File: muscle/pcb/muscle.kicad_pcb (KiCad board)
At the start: 4 copper layers, 135 x 50 mm, 176 parts, among them J1 B4B-XH-2(LF)(SN), J10 USB4115-03-C, J2 WAFER-SH1.0-3PWB, J4 WAFER-SH1.0-3PWB, J5 B4B-XH-2(LF)(SN), J8 B2B-XH-A(LF)(SN), J9 USB4115-03-C, Q1 AO3401A, Q10 BSS138W, Q2 AONR21321, Q3 WSD6070DN56, Q4 WSD6070DN56, Q5 BSS138W, Q6 WSD6070DN56, Q7 AONR21321, Q8 WSD6070DN56, Q9 AGM18N10AP, SW1 TS3425BA, SW2 TS3425BA, U1 TMC2209-LA, U11 TPS563300, U13 TLV75733PDBV, U14 DRV8701P, U2 TMC2209-LA, U3 RP2350A, U4 CYPD3177-24LQ, U5 LM5156, U6 W25Q128JVSS, U7 LM393BIDSGR, U8 TUSB320, U9 TPS2041BDBV, Y1 ABM8-272-T3

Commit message: muscle: switch to side buttons for RESET and BOOT
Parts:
- SW1, SW2: value TS3425BA -> TS24CA; footprint Button_Switch_SMD:SW_Push_1P1T_NO_Vertical_Wuerth_434133025816 -> Button_Switch_SMD:Panasonic_EVQPUL_EVQPUC
- moved J2 17.6 mm to (194.7, 95.6)
- moved R7 12.6 mm to (188.4, 116.0)
- moved R19 11.8 mm to (192.5, 109.2), turned to -90 degrees
- moved SW1 10.2 mm to (195.5, 113.5), turned to -90 degrees
- moved R13 9.97 mm to (187.2, 116.0)
- moved SW2 9.29 mm to (195.5, 105.5)
- moved R18 5.20 mm to (182.3, 94.6), turned to 180 degrees
- moved J4 1.85 mm to (194.7, 88.0)
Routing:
- net /QSPI_SS: track 44.9 -> 19.5 mm, vias 2 -> 0
- net /DBG_TX: track 8.14 -> 22.8 mm
- net /RESET: track 36.2 -> 46.8 mm, vias 2 -> 4
- net /~{USB_BOOT}: track 5.59 -> 15.0 mm, vias 0 -> 2
- net /DBG_RX: track 12.9 -> 18.4 mm
- net GND: track 159.2 -> 161.5 mm, vias 228 -> 227
- net /SWCLK: track 27.3 -> 28.1 mm
- net /SWD: track 28.3 -> 29.1 mm
- net /S_SENSE_COMP: track 9.68 -> 9.00 mm
- net Net-(U1-VREF): track 10.5 -> 9.90 mm

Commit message: muscle: use correct TUSB320LI model
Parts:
- U8: value TUSB320 -> TUSB320LI
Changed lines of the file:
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@@
 			)
 		)
-		(property "Value" "TUSB320"
+		(property "Value" "TUSB320LI"
 			(at 0.05 1.025 0)
 			(layer "F.Fab")
@@
 			)
 		)
-		(property "Datasheet" "http://www.ti.com/lit/ds/symlink/tusb320.pdf"
+		(property "Datasheet" "https://www.ti.com/lit/ds/symlink/tusb320li.pdf"
 			(at 0 0 0)
 			(layer "F.Fab")
@@
 			(hide yes)
 			(effects
+				(font
+					(size 1 1)
+					(thickness 0.15)
+				)
+			)
+		)
+		(property "LCSC" "C2836598"
+			(at 0 0 0)
+			(unlocked yes)
+			(layer "F.Fab")
+			(hide yes)
+			(effects

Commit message: muscle: USB protection
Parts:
- added U12: TPD2EUSB30A, Package_TO_SOT_SMD:Texas_DRT-3, F.Cu at (98.0, 100.2)
- moved R33 2.25 mm to (98.0, 97.3)
- moved D6 1.22 mm to (92.1, 97.3)
- moved C41 1.17 mm to (95.2, 94.3)
- moved U9 1.17 mm to (95.2, 97.0)
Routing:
- net /USB_D-: track 99.8 -> 107.1 mm
- net /USB_D+: track 103.2 -> 107.3 mm
- net GND: track 161.5 -> 164.4 mm, vias 227 -> 226
- net /USB_ROLE: track 104.3 -> 105.7 mm
- net /VBUS_DATA: track 25.6 -> 27.0 mm
- net +3V3: track 161.0 -> 159.7 mm
- net +5V: track 38.3 -> 39.5 mm
- net /~{DRV_EN}: track 130.4 -> 129.5 mm
- net /RESET: track 46.8 -> 46.0 mm
- net Net-(R19-Pad1): track 9.90 -> 9.32 mm

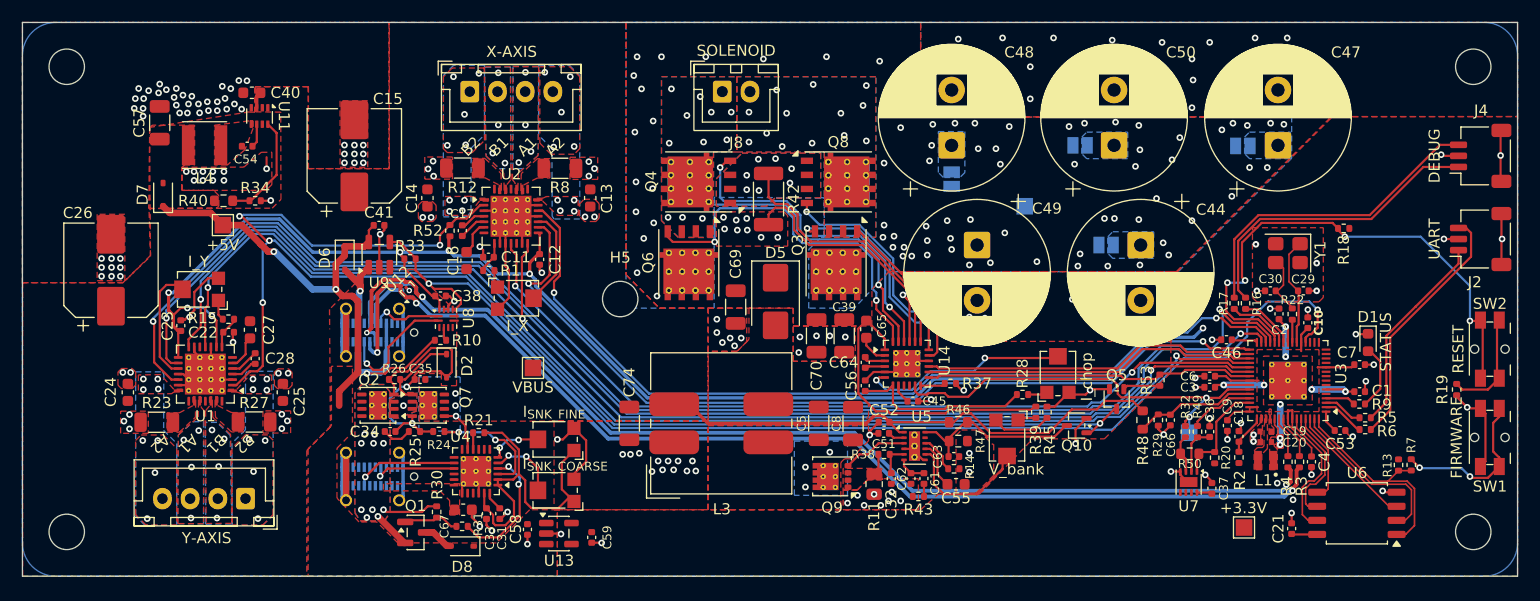
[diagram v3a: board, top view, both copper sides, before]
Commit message: muscle: replace USB PD power
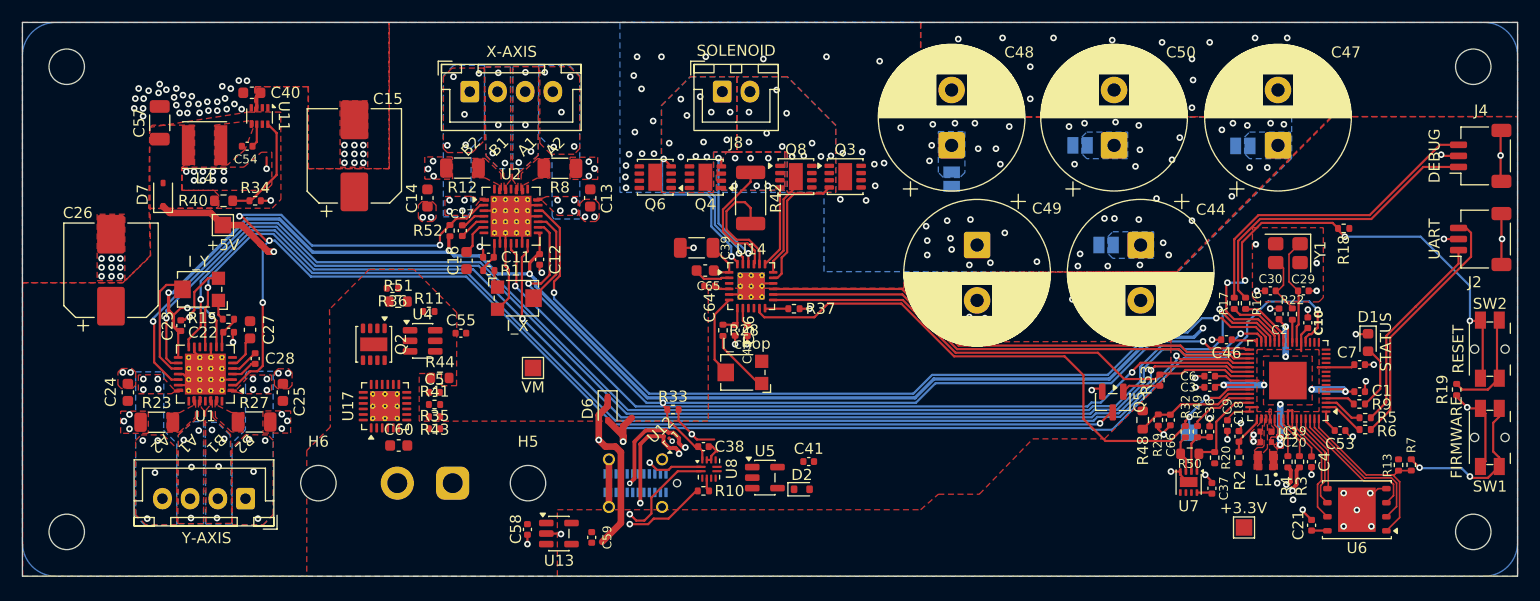
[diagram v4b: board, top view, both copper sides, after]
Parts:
- removed C31, C34, C35, C51, C52, C61: 1u, Capacitor_SMD:C_0402_1005Metric
- removed C32, C63: 100p, Capacitor_SMD:C_0402_1005Metric
- removed C33: 4.7u, Capacitor_SMD:C_0402_1005Metric
- removed C62: 22n, Capacitor_SMD:C_0402_1005Metric
- removed C67: 10u, Capacitor_SMD:C_0603_1608Metric
- removed C69, C70, C74: 10u, Capacitor_SMD:C_1206_3216Metric
- removed C8: 4.7u, Capacitor_SMD:C_1206_3216Metric
- removed D5: 100V,5A, Diode_SMD:D_SMB
- removed D8: ~, Diode_SMD:D_SOD-323
- removed J9: USB4115-03-C, Connector_USB:USB_C_Receptacle_GCT_USB4115-03-C
- removed L3: 33u,2.4A, Inductor_SMD:L_Bourns_SRF1260
- removed Q1: AO3401A, Package_TO_SOT_SMD:SOT-23
- removed Q10: BSS138W, Package_TO_SOT_SMD:SOT-323_SC-70
- removed Q7: AONR21321, Package_DFN_QFN:DFN-8-1EP_3x3mm_P0.65mm_EP1.6x2.56mm_ThermalVias
- removed Q9: AGM18N10AP, mainboard:VSON-8_3.3x3.3mm_P0.65mm_NexFET_Thermalvias
- removed R14: 51k, Resistor_SMD:R_0402_1005Metric
- removed R21, R26, R30: 50k, Resistor_SMD:R_0402_1005Metric
- removed R24, R31: 1k, Resistor_SMD:R_0402_1005Metric
- removed R25: 10k, Resistor_SMD:R_0402_1005Metric
- removed R38: 100, Resistor_SMD:R_0402_1005Metric
- removed R39: 200k, Resistor_SMD:R_0402_1005Metric
- removed R45: 5.1k, Resistor_SMD:R_0402_1005Metric
- removed R46: 68k, Resistor_SMD:R_0603_1608Metric
- removed R47: 6.8k, Resistor_SMD:R_0603_1608Metric
- removed RV3: V_bank, Potentiometer_SMD:Potentiometer_Bourns_TC33X_Vertical
- removed RV4: I_{SNK_COARSE}, Potentiometer_SMD:Potentiometer_Bourns_TC33X_Vertical
- removed RV5: I_{SNK_FINE}, Potentiometer_SMD:Potentiometer_Bourns_TC33X_Vertical
- removed TP4: VS, TestPoint:TestPoint_Pad_1.5x1.5mm
- removed U9: TPS2041BDBV, Package_TO_SOT_SMD:SOT-23-5
- added C60: 1u, Capacitor_SMD:C_0603_1608Metric, F.Cu at (97.0, 114.2)
- added H6: MountingHole, MountingHole:MountingHole_3.2mm_M3_DIN965, F.Cu at (89.7, 117.6)
- added J3: XT30UPB-M, Connector_AMASS:AMASS_XT30UPB-M_1x02_P5.0mm_Vertical, B.Cu at (101.8, 117.6)
- added R35: 348k, Resistor_SMD:R_0402_1005Metric, F.Cu at (100.2, 112.7)
- added R36: 348k, Resistor_SMD:R_0402_1005Metric, F.Cu at (96.4, 100.0)
- added R41: 15k, Resistor_SMD:R_0402_1005Metric, F.Cu at (100.2, 110.5)
- added R44: 3.9k, Resistor_SMD:R_0603_1608Metric, F.Cu at (100.7, 108.1)
- added R51: 68k, Resistor_SMD:R_0603_1608Metric, F.Cu at (96.9, 101.2)
- added U17: TPS16630RGE, Package_DFN_QFN:Texas_RGE0024H_VQFN-24-1EP_4x4mm_P0.5mm_EP2.7x2.7mm_ThermalVias, F.Cu at (95.7, 110.7)
- C5: value 4.7u -> 1u; footprint Capacitor_SMD:C_1206_3216Metric -> Capacitor_SMD:C_0402_1005Metric
- C55: value 470n -> 100n; footprint Capacitor_SMD:C_0603_1608Metric -> Capacitor_SMD:C_0402_1005Metric
- D2: value 12V -> ~; footprint Diode_SMD:D_SOD-323 -> Diode_SMD:D_SOD-523
- Q2: value AONR21321 -> WSD4070DN33; footprint Package_DFN_QFN:DFN-8-1EP_3x3mm_P0.65mm_EP1.6x2.56mm_ThermalVias -> mainboard:Winsok_DFN-8-1EP_3x3mm_P0.65mm_EP1.25x2.45mm
- Q3, Q4, Q6, Q8: footprint mainboard:WSD_DFN-8-1EP_6x5mm_P1.27mm_ThermalVias -> mainboard:Winsok_DFN-8-1EP_3x3mm_P0.65mm_EP1.25x2.45mm
- Q5: footprint Package_TO_SOT_SMD:SOT-323_SC-70 -> Package_TO_SOT_SMD:SOT-23
- R11: value 33m,0.5W -> 100; footprint Resistor_SMD:R_0805_2012Metric -> Resistor_SMD:R_0402_1005Metric
- R43: value 10k -> 15k
- TP3: value VBUS -> VM
- U3: footprint Package_DFN_QFN:QFN-60-1EP_7x7mm_P0.4mm_EP3.4x3.4mm_ThermalVias -> Package_DFN_QFN:QFN-60-1EP_7x7mm_P0.4mm_EP3.4x3.4mm
- U4: value CYPD3177-24LQ -> LM5050-1; footprint Package_DFN_QFN:QFN-24-1EP_4x4mm_P0.5mm_EP2.75x2.75mm_ThermalVias -> Package_TO_SOT_SMD:TSOT-23-6
- U5: value LM5156 -> TPS2061CDBV; footprint Package_SON:WSON-12-1EP_3x2mm_P0.5mm_EP1x2.65_ThermalVias -> Package_TO_SOT_SMD:SOT-23-5
- U6: value W25Q128JVSS -> XT25F128FWOIGT-W; footprint Package_SO:SOIC-8_5.3x5.3mm_P1.27mm -> Package_SON:WSON-8-1EP_6x5mm_P1.27mm_EP3.4x4mm
- moved C55 46.7 mm to (102.6, 104.1)
- moved R43 44.3 mm to (100.2, 111.6)
- moved C41 44.3 mm to (134.0, 115.7)
- moved R11 43.1 mm to (99.7, 102.1), turned to 0 degrees
- moved C5 34.8 mm to (100.2, 109.4), turned to 0 degrees
- moved D2 34.0 mm to (133.4, 118.2), turned to 0 degrees
- moved RV2 28.5 mm to (128.0, 107.6), turned to 180 degrees
- moved R28 27.7 mm to (126.2, 103.8), turned to -90 degrees
- moved D6 27.4 mm to (115.8, 110.9)
- moved R33 27.4 mm to (121.7, 111.0)
- moved U12 27.4 mm to (121.7, 113.8)
- moved U8 27.4 mm to (125.0, 116.3)
- moved C38 27.4 mm to (124.5, 114.3)
- moved J10 27.4 mm to (118.4, 117.6)
- moved R10 27.4 mm to (124.5, 118.3)
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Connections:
- net /VBUS_SENSE renamed /VM_SENSE
- C13 pad 1: VBUS -> VM
- C14 pad 1: VBUS -> VM
- C15 pad 1: VBUS -> VM
- C16 pad 1: VBUS -> VM
- C24 pad 1: VBUS -> VM
- C25 pad 1: VBUS -> VM
- C26 pad 1: VBUS -> VM
- C27 pad 2: VBUS -> VM
- C39 pad 1: VS -> VM
- C40 pad 1: VBUS -> VM
- C41 pad 1: +5V -> VBUS_SW
- C49 pad 1: VS -> VM
- C5 pad 2: Net-(D5-A) -> GND
- C55 pad 1: Net-(U5-SS) -> Net-(U4-VS)
- C57 pad 1: Net-(D7-A) -> VBUS_SW
- C65 pad 1: VS -> VM
- D2 pad 1: Net-(D2-K) -> GND
- D2 pad 2: Net-(D2-A) -> VBUS
- D6 pad 2: /VBUS_DATA -> VBUS
- D7 pad 2: Net-(D7-A) -> VBUS_SW
- J10 pad A4: /VBUS_DATA -> VBUS
- J10 pad A9: /VBUS_DATA -> VBUS
- J10 pad B4: /VBUS_DATA -> VBUS
- J10 pad B9: /VBUS_DATA -> VBUS
- JP11 pad 1: VS -> VM
- JP12 pad 1: VS -> VM
- JP13 pad 1: VS -> VM
- JP14 pad 1: VS -> VM
- L4 pad 2: Net-(D7-A) -> VBUS_SW
- Q2 pad 1: Net-(D2-K) -> VM
- Q2 pad 2: Net-(D2-K) -> VM
- Q2 pad 3: Net-(D2-K) -> VM
- Q2 pad 4: Net-(D2-A) -> Net-(Q2-G)
- Q2 pad 5: VBUS0 -> Net-(U4-IN)
- Q2 pad 6: VBUS0 -> Net-(U4-IN)
- Q2 pad 7: VBUS0 -> Net-(U4-IN)
- Q2 pad 8: VBUS0 -> Net-(U4-IN)
- Q2 pad 9: VBUS0 -> Net-(U4-IN)
- Q3 pad 5: VS -> VM
- Q6 pad 5: VS -> VM
- R10 pad 1: /VBUS_DATA -> VBUS
- R11 pad 1: Net-(Q9-S-Pad1) -> VM
- R11 pad 2: GND -> Net-(U4-VS)
- R40 pad 1: Net-(D7-A) -> VBUS_SW
- R43 pad 2: GND -> Net-(U17-OVP)
- R48 pad 1: VBUS -> VM
- TP3 pad 1: VBUS -> VM
- U1 pad 22: VBUS -> VM
- U1 pad 28: VBUS -> VM
- U11 pad 2: unconnected-(U11-EN-Pad2) -> /PWR_EN
- U11 pad 3: VBUS -> VM
- U14 pad 1: VS -> VM
- U2 pad 22: VBUS -> VM
- U2 pad 28: VBUS -> VM
- U4 pad 1: /PD_VDDD -> Net-(U4-VS)
- U4 pad 2: /PD_VDDD -> GND
- U4 pad 3: Net-(U4-VBUS_FET_EN) -> GND
- U4 pad 4: Net-(U4-SAFE_PWR_EN) -> Net-(U4-IN)
- U4 pad 5: /ISNK_COARSE -> Net-(Q2-G)
- U4 pad 6: /ISNK_FINE -> VM
- U5 pad 2: Net-(U5-VCC) -> GND
- U5 pad 3: Net-(Q9-G) -> unconnected-(U5-~{FLT}-Pad3)
- U5 pad 4: GND -> /USB_ROLE
- U5 pad 5: Net-(U5-CS) -> VBUS_SW
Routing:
- net /USB_D-: track 107.1 -> 12.0 mm
- net /USB_D+: track 107.3 -> 12.8 mm
- net GND: track 164.4 -> 102.1 mm, vias 226 -> 182
- net VBUS: track 52.4 -> 12.1 mm, vias 3 -> 2
- net /PD_VDDD: track 30.2 -> 0.00 mm
- net /USB_ROLE: track 105.7 -> 78.0 mm
- net VS: track 27.2 -> 0.00 mm, vias 77 -> 0
- net /VBUS_DATA: track 27.0 -> 0.00 mm, vias 2 -> 0
- net Net-(D2-A): track 26.3 -> 0.00 mm, vias 2 -> 0
- net /S_SENSE: track 37.9 -> 56.5 mm
- net /S2: track 26.5 -> 8.33 mm
- net Net-(Q4-G): track 29.7 -> 11.5 mm
- net Net-(Q6-G): track 33.0 -> 15.6 mm
- net /DRV_EN: track 29.7 -> 46.5 mm
- net /S_EN: track 15.8 -> 0.00 mm
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- added copper zone on F.Cu, net VBUS_SW
- added copper zone on B.Cu, net VM
- added copper zone on F.Cu, net VM
- added copper zone on In1.Cu, net VM
- added copper zone on In2.Cu, net VM
- removed copper zone on F.Cu, net +5V
- removed copper zone on B.Cu, net Net-(D2-K)
- removed copper zone on F.Cu, net Net-(D2-K)
- removed copper zone on In1.Cu, net Net-(D2-K)
- removed copper zone on In2.Cu, net Net-(D2-K)
- removed copper zone on F.Cu, net Net-(D5-A)
- removed copper zone on F.Cu, net Net-(D7-A)
- removed copper zone on F.Cu, net Net-(Q9-S-Pad1)
- removed copper zone on B.Cu, net Net-(U17-dVdT)
- removed copper zone on F.Cu, net Net-(U17-dVdT)
- removed copper zone on B.Cu, net VBUS
- removed copper zone on F.Cu, net VBUS
- removed copper zone on B.Cu, net VBUS0
- removed copper zone on F.Cu, net VBUS0
- removed copper zone on In1.Cu, net VBUS0
- removed copper zone on In2.Cu, net VBUS0
- removed copper zone on B.Cu, net VS
- removed copper zone on F.Cu, net VS
- removed copper zone on In1.Cu, net VS
- removed copper zone on In2.Cu, net VS

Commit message: muscle: changed to TPS16330PWP
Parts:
- U17: footprint Package_DFN_QFN:Texas_RGE0024H_VQFN-24-1EP_4x4mm_P0.5mm_EP2.7x2.7mm_ThermalVias -> Package_SO:HTSSOP-20-1EP_4.4x6.5mm_P0.65mm_EP3.4x6.5mm_Mask2.96x2.96mm_ThermalVias
- moved R41 3.42 mm to (103.4, 109.3)
- moved U17 3.42 mm to (99.0, 109.5)
- moved R35 3.42 mm to (103.4, 111.5)
- moved R43 3.42 mm to (103.4, 110.5)
- moved C5 3.42 mm to (103.4, 108.2)
- moved R44 3.42 mm to (103.9, 107.0)
- moved Q2 1.85 mm to (94.7, 103.2)
- moved C55 1.15 mm to (102.6, 102.9)
- moved R36 1.15 mm to (96.4, 98.8)
- moved R51 1.15 mm to (96.9, 100.0)
- moved U4 1.15 mm to (99.1, 103.6)
- moved R11 1.15 mm to (99.7, 101.0)
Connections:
- U17 pad 10: Net-(U17-ILIM) -> Net-(U17-dVdT)
- U17 pad 11: GND -> Net-(U17-ILIM)
- U17 pad 12: unconnected-(U17-~{SHDN}-Pad12) -> GND
- U17 pad 14: GND -> unconnected-(U17-IMON-Pad14)
- U17 pad 15: unconnected-(U17-NC-Pad15) -> GND
- U17 pad 17: Net-(U4-IN) -> unconnected-(U17-NC-Pad17)
- U17 pad 19: GND -> Net-(U4-IN)
- U17 pad 20: GND -> Net-(U4-IN)
- U17 pad 3: unconnected-(U17-NC-Pad3) -> Net-(J3-N)
- U17 pad 5: Net-(J3-N) -> unconnected-(U17-NC-Pad5)
- U17 pad 6: Net-(U17-UVLO) -> Net-(J3-N)
- U17 pad 7: Net-(U17-OVP) -> Net-(U17-UVLO)
- U17 pad 8: GND -> Net-(U17-OVP)
- U17 pad 9: Net-(U17-dVdT) -> GND

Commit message: muscle,seed: wip
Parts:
- removed H6: MountingHole, MountingHole:MountingHole_3.2mm_M3_DIN965
- moved C38 28.1 mm to (152.6, 114.3)
- moved R10 28.1 mm to (152.6, 118.3)
- moved R33 28.1 mm to (149.8, 111.0)
- moved U8 28.1 mm to (153.1, 116.3)
- moved C41 28.1 mm to (162.1, 115.7)
- moved C58 28.1 mm to (136.7, 121.8)
- moved C59 28.1 mm to (142.5, 122.5)
- moved D2 28.1 mm to (161.5, 118.2)
- moved D6 28.1 mm to (143.9, 110.9)
- moved J10 28.1 mm to (146.5, 117.6)
- moved U12 28.1 mm to (149.8, 113.8)
- moved U13 28.1 mm to (139.5, 122.2)
- moved U5 28.1 mm to (158.1, 117.1)
- moved C60 4.77 mm to (93.4, 111.1), turned to 90 degrees
- moved J3 2.00 mm to (99.8, 117.6)
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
